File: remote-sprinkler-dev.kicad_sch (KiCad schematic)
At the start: 20 parts, among them J1 CN7, J2 CN10, J3 Conn_01x02, Q3 BSD840N, Q4 DMG2302U, U1 DMHC3025LSD-13

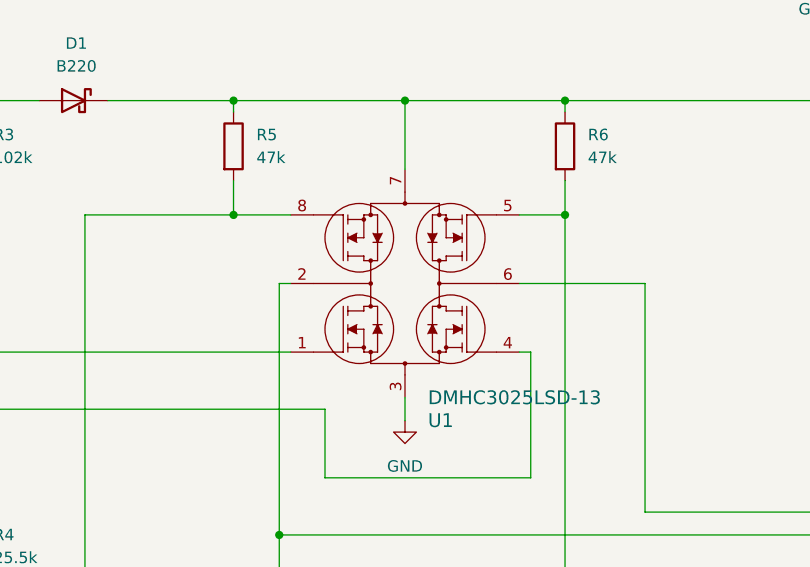
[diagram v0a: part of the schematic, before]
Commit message: Changed transistor library
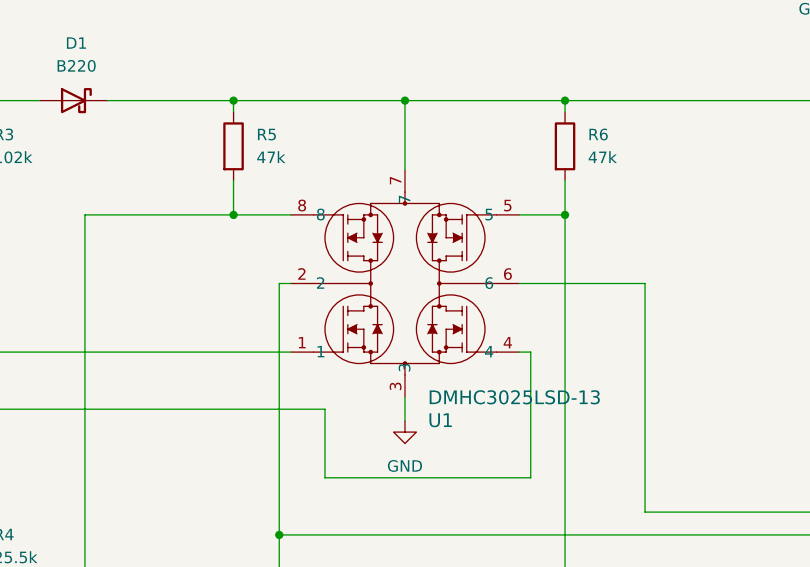
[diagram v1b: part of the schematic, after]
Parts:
- U1: symbol XSTR:DMHC3025LSD-13 -> XSR:DMHC3025LSD-13
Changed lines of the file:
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@@
 	)
 	(symbol
-		(lib_id "XSTR:DMHC3025LSD-13")
+		(lib_id "XSR:DMHC3025LSD-13")
 		(at 175.26 73.66 0)
 		(unit 1)

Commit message: added heirarchy
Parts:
- U1: symbol XSR:DMHC3025LSD-13 -> XTR:DMHC3025LSD-13
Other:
- added sheet Voltage Booster (voltage-boost.kicad_sch)
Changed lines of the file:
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@@
 	)
 	(symbol
-		(lib_id "XSR:DMHC3025LSD-13")
+		(lib_id "XTR:DMHC3025LSD-13")
 		(at 175.26 73.66 0)
 		(unit 1)
@@
 		)
 		(property "Footprint" "soic127p610x495-8n"
-			(at 177.8 67.31 0)
+			(at 175.26 73.66 0)
 			(effects
 				(font
@@
 		)
 		(property "Datasheet" "https://www.diodes.com/assets/Datasheets/DMHC3025LSD.pdf"
-			(at 191.008 60.198 0)
+			(at 175.26 73.66 0)
 			(effects
 				(font
@@
 			)
 		)
-		(property "Description" ""
+		(property "Description" "Dual N/P Channel 30 V 25 mO 11.7 nC H-Bridge Power Mosfet - SOIC-8"
 			(at 175.26 73.66 0)
 			(effects
@@
 		(on_board yes)
 		(dnp no)
-		(fields_autoplaced yes)
 		(property "Reference" "R1"
 			(at 176.53 115.5699 0)
@@
 				)
 			)
+		)
+	)
+	(sheet
+		(at 179.07 21.59)
+		(size 36.83 29.21)
+		(exclude_from_sim no)
+		(in_bom yes)
+		(on_board yes)
+		(dnp no)
+		(fields_autoplaced yes)
+		(stroke
+			(width 0.1524)
+			(type solid)
+		)
+		(fill
+			(color 0 0 0 0.0000)
+		)
+		(property "Sheetname" "Voltage Booster"
+			(at 179.07 20.8784 0)
+			(effects
+				(font
+					(size 1.27 1.27)
+				)
+				(justify left bottom)
+			)
+		)
+		(property "Sheetfile" "voltage-boost.kicad_sch"
+			(at 179.07 51.3846 0)
+			(effects
+				(font
+					(size 1.27 1.27)
+				)
+				(justify left top)
+			)
+		)
+		(instances
+			(project "remote-sprinkler-dev"
+				(path "/da5a1e6a-2605-436b-a30c-1027586d5c0a"
+					(page "2")
+				)
+			)
